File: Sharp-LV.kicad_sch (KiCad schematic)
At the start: 46 parts, among them J1 USB_C_Receptacle_USB2.0, J2 Conn_01x05_PROG, J3 5024260810, J4 FH52-10S-0.5SH_99, J5 SM04B-SRSS-TB_LF__SN_, J6 Conn_2Rows-13Pins, U1 NRF52840-QIAA-R, U2 USBLC6-2P6, U3 MCP1700-3302E_SOT23, U4 RT9080-33GJ5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

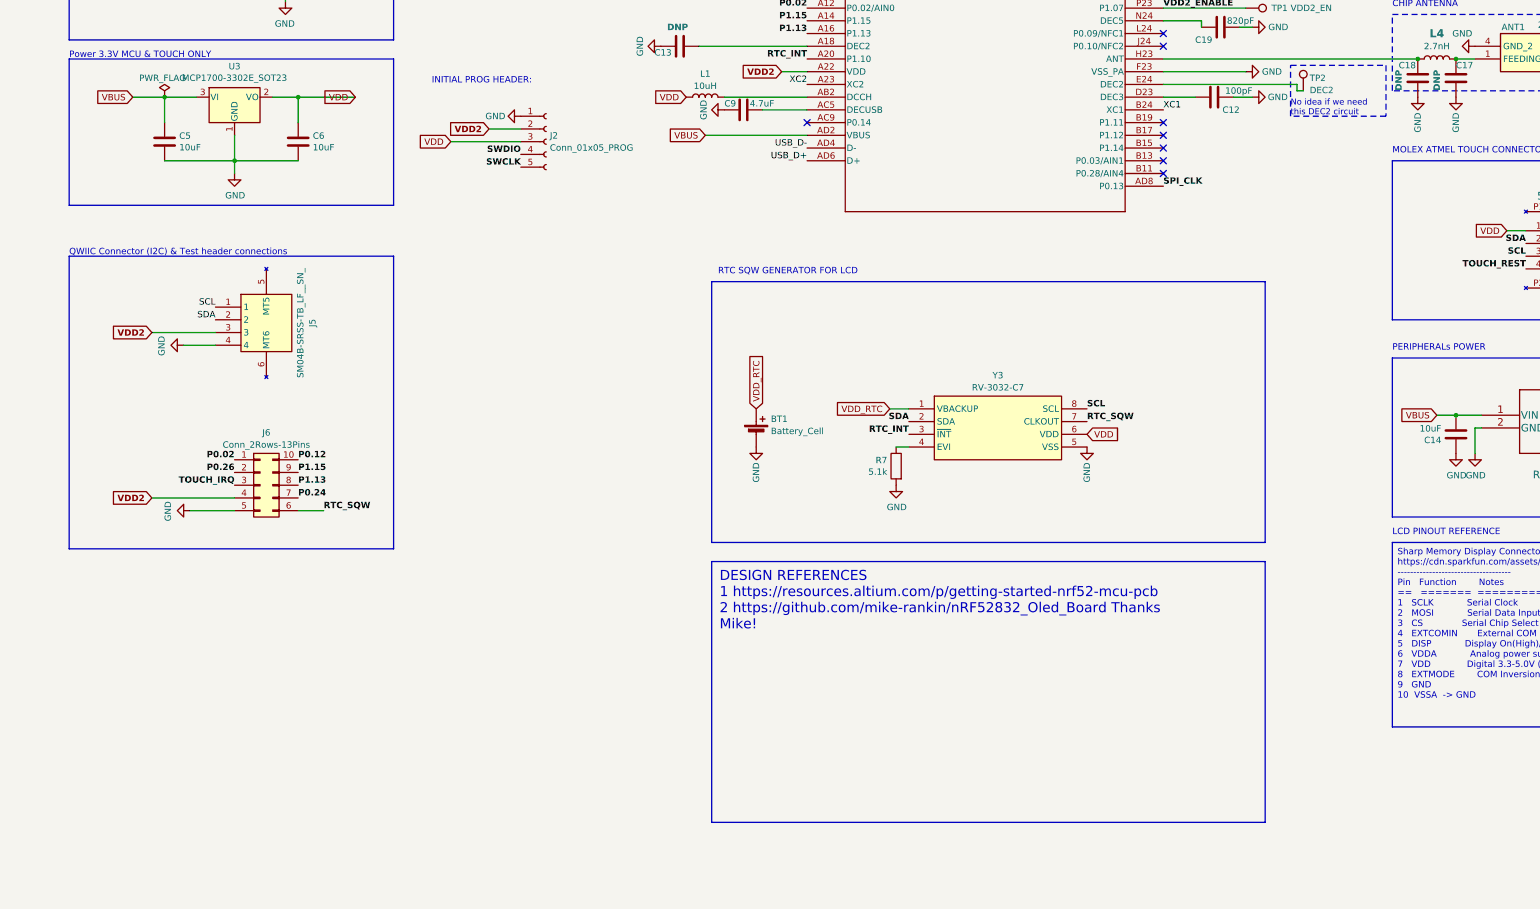
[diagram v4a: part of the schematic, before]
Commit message: Add power mux TPS2113
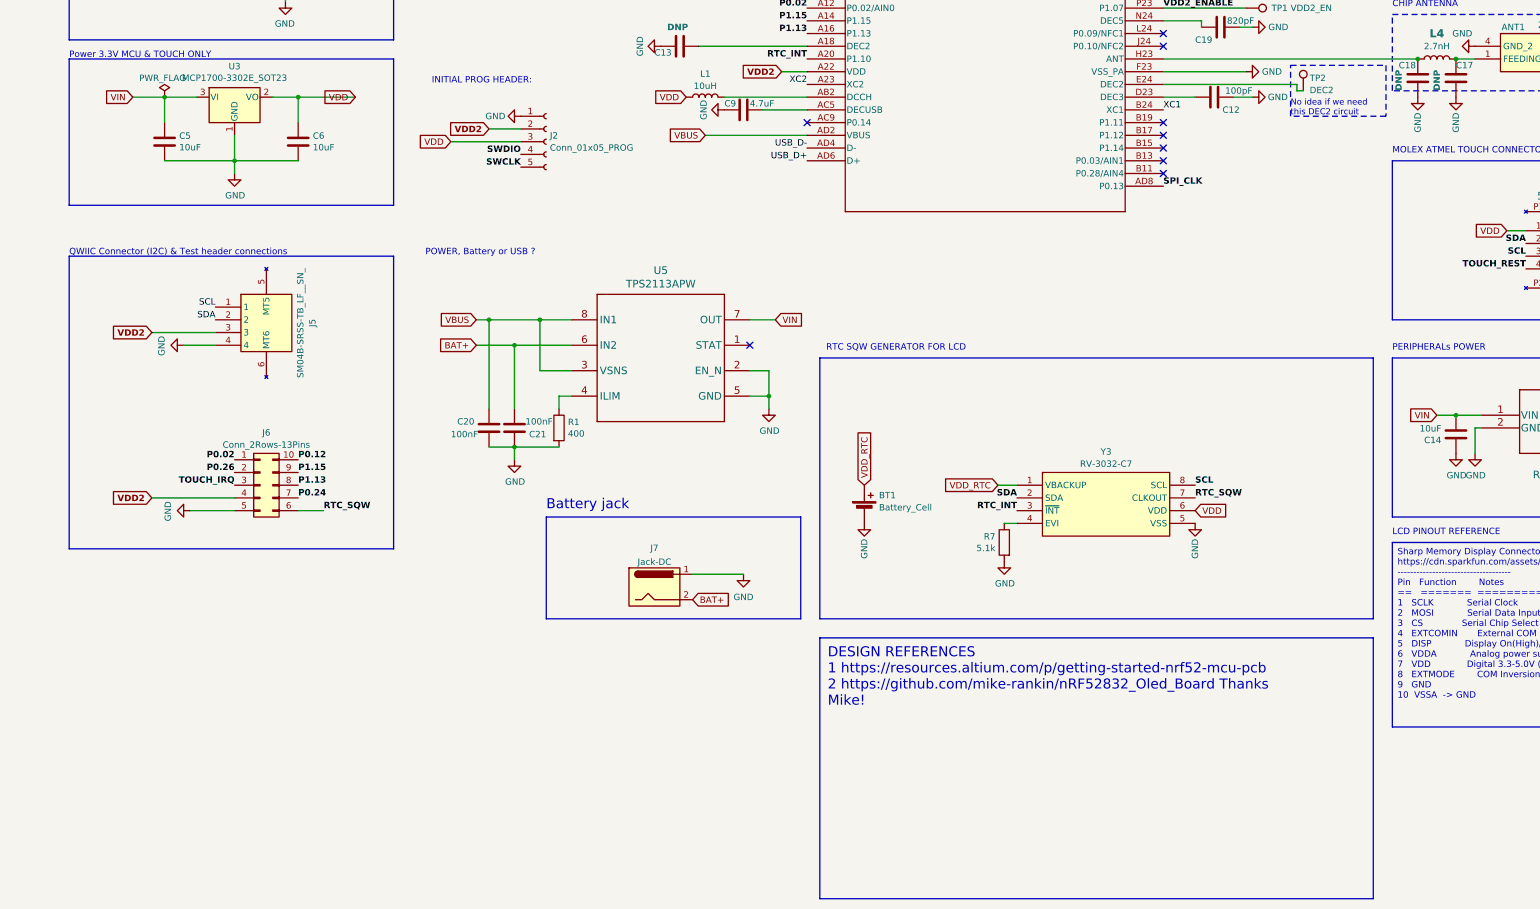
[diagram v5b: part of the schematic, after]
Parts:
- added C20, C21: 100nF, Capacitor_SMD:C_0805_2012Metric, symbol Device:C
- added J7: Jack-DC, Connector_JST:JST_LEA_SM02B-LEASS-TF_1x02-1MP_P4.20mm_Horizontal, symbol Connector:Jack-DC
- added R1: 400, Resistor_SMD:R_0603_1608Metric, symbol Device:R
- added U5: TPS2113APW, Footprints:TPS2113APWR, symbol epd_breakout:TPS2113APW
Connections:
- net GND: now also C20.2, C21.1, J7.1, R1.2, U5.2 (EN_N), U5.5 (GND)
- net VBUS: now also C20.1, U5.3 (VSNS), U5.8 (IN1); no longer C14.1, C5.2, U3.3 (VI), U4.1 (VIN)
- new net: R1.1, U5.4 (ILIM)
- new net BAT+: C21.2, J7.2, U5.6 (IN2)
- new net VIN: C14.1, C5.2, U3.3 (VI), U4.1 (VIN), U5.7 (OUT)
- no-connect marks 36 -> 37
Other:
- note added: "Battery jack"
- note added: "POWER, Battery or USB ?"
- moved on the sheet: BT1, R7, Y3

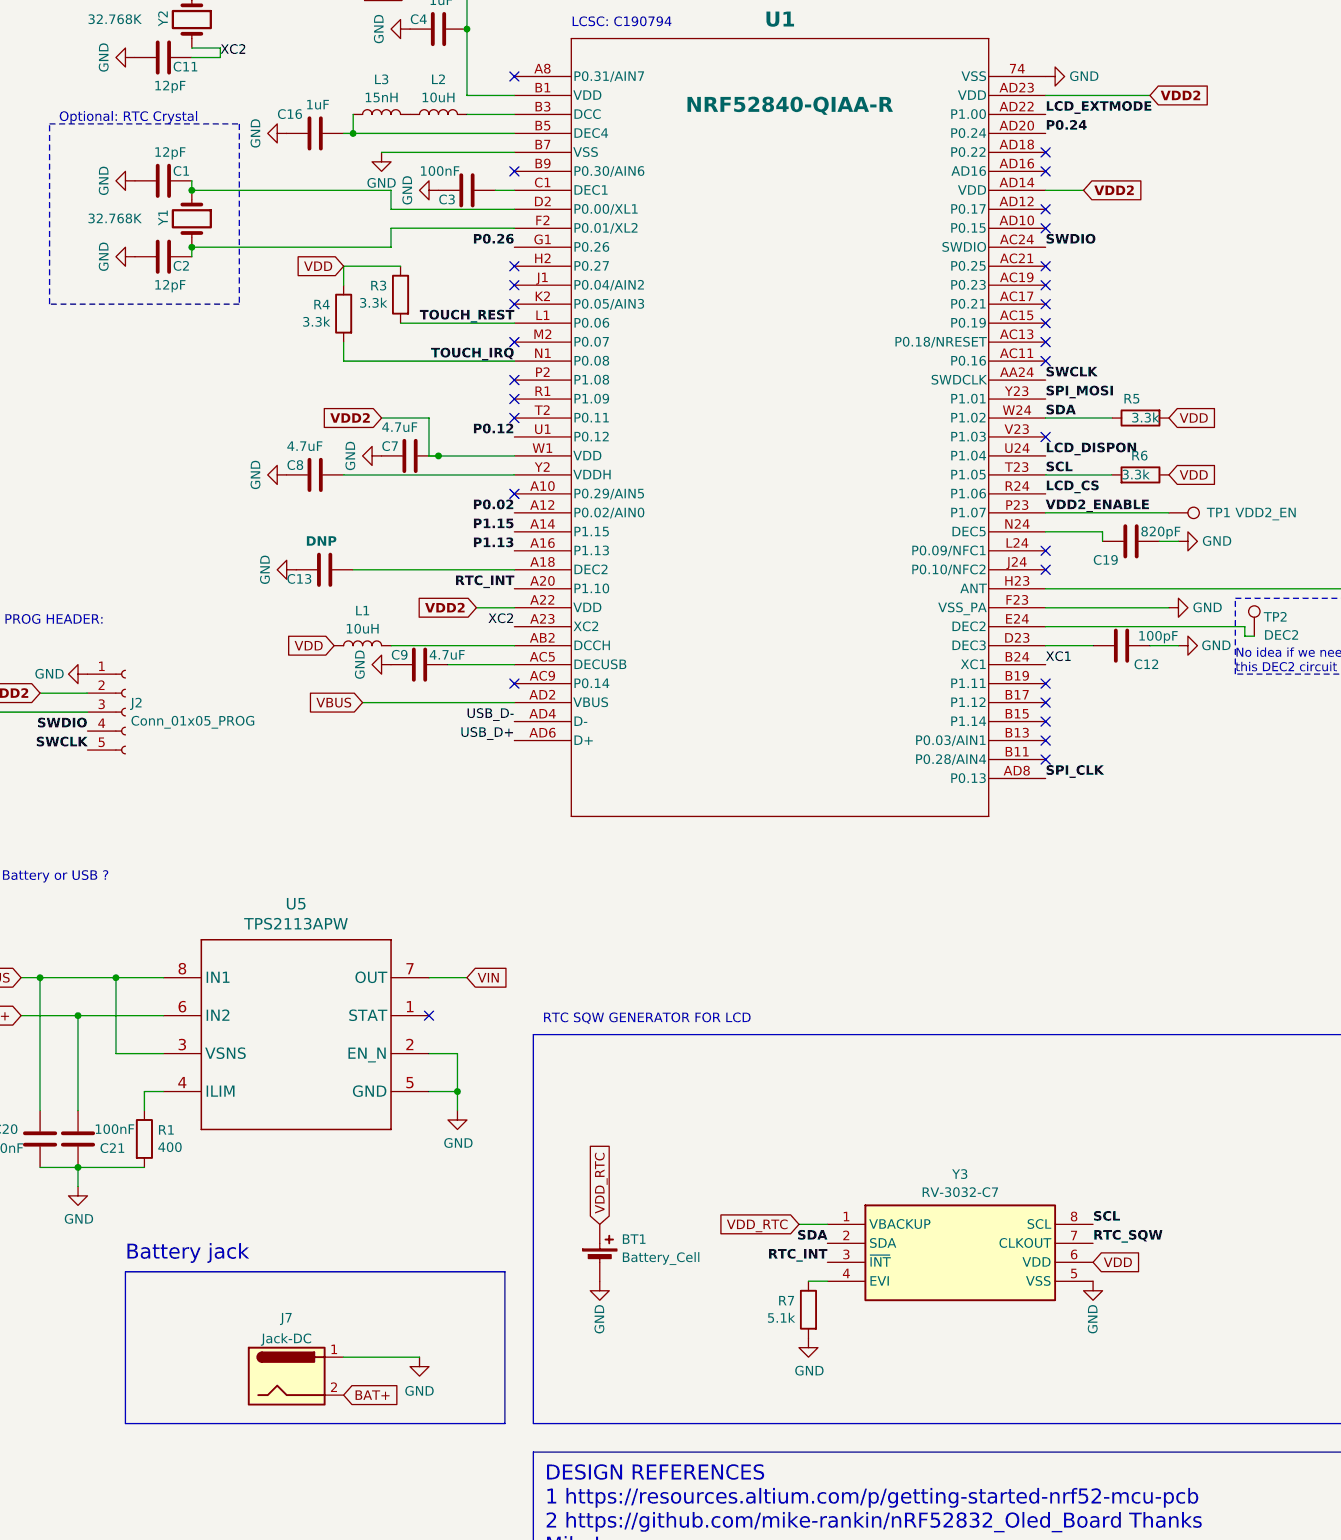
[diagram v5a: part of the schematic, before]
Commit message: Update battery connector & add SCH pdf
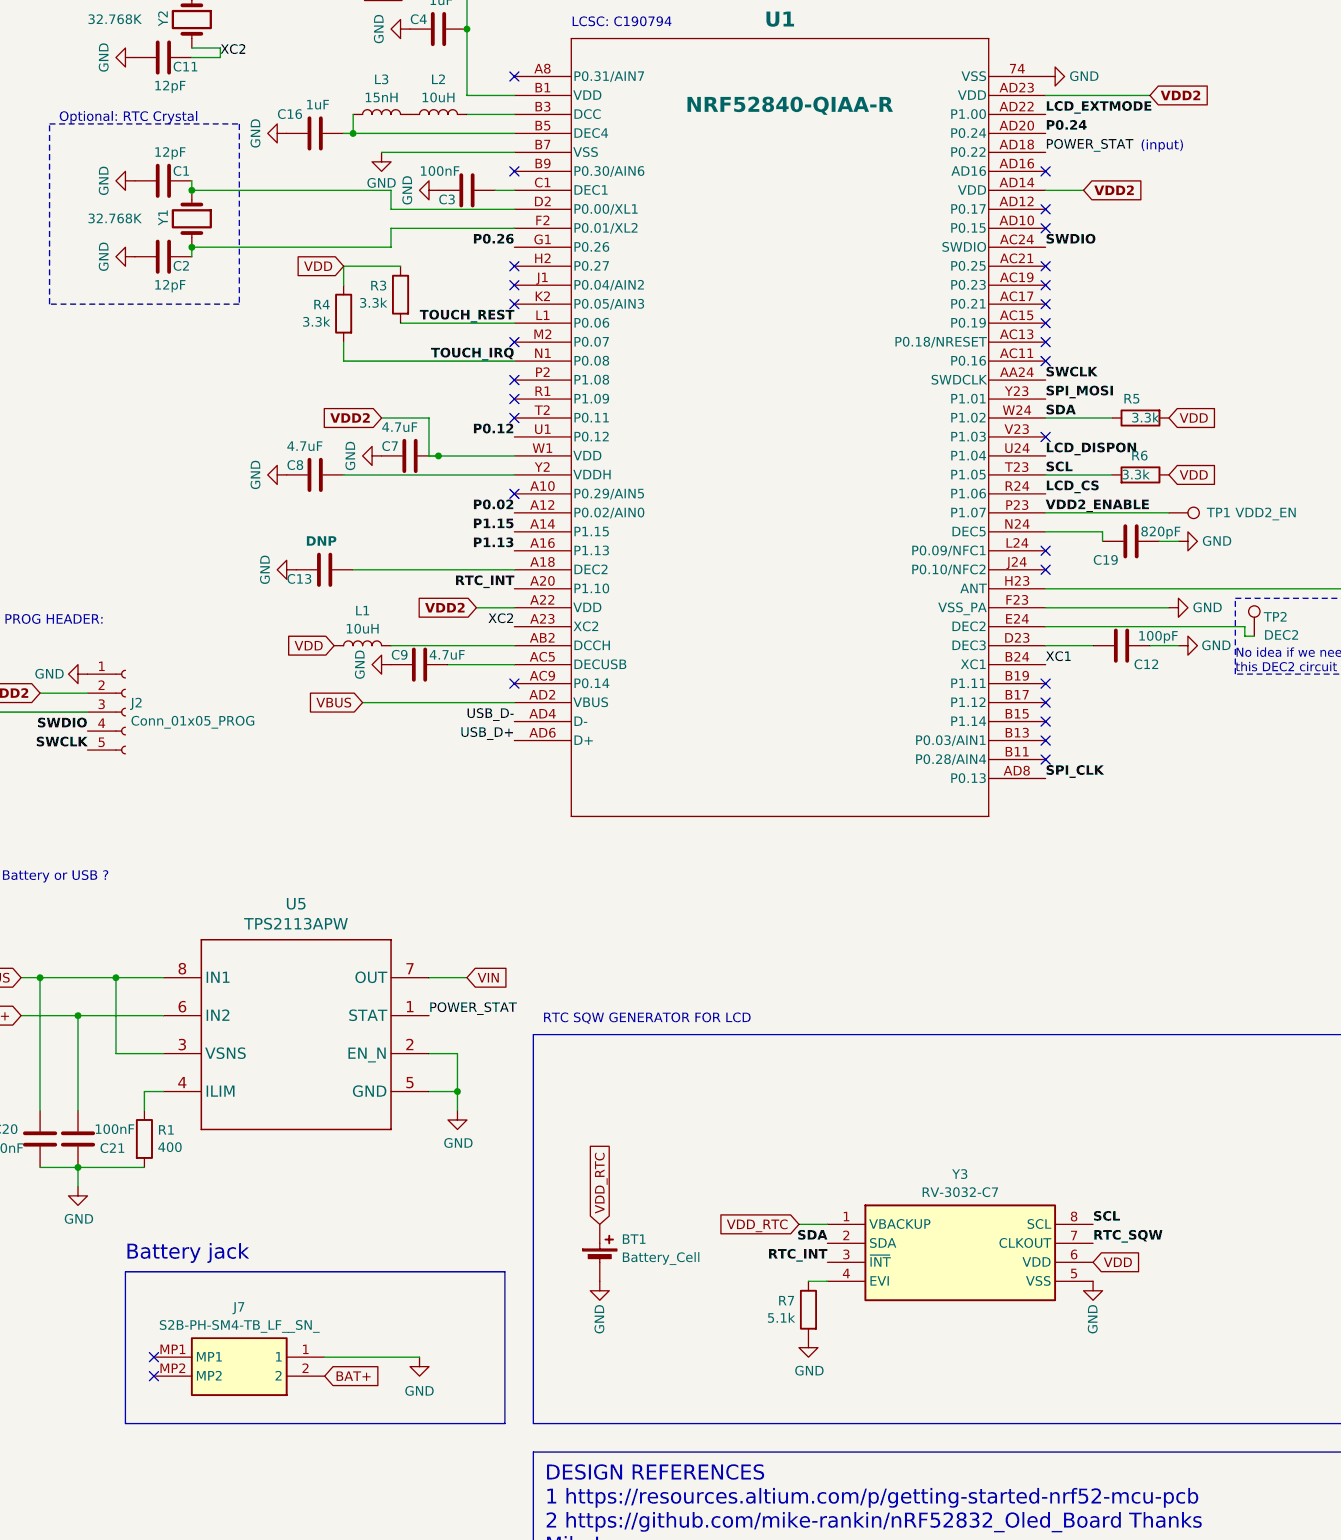
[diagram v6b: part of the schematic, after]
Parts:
- removed J7: Jack-DC, Connector_JST:JST_LEA_SM02B-LEASS-TF_1x02-1MP_P4.20mm_Horizontal, symbol Connector:Jack-DC
- added J7: S2B-PH-SM4-TB_LF__SN_, Footprints:S2BPHSM4TBLFSN, symbol Battery:S2B-PH-SM4-TB_LF__SN_
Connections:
- net BAT+: now also J7.2
- net GND: now also J7.1
- net POWER_STAT: now reaches U5.1 (STAT)
- net POWER_STAT: now also U1.AD18 (P0.22)
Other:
- note added: "(input)"
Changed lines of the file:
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@@
   (no_connect (at 251.46 80.01))
   (no_connect (at 341.63 152.4))
+  (no_connect (at 132.08 218.44))
+  (no_connect (at 132.08 215.9))
   (no_connect (at 251.46 125.73))
-  (no_connect (at 168.91 170.18))
   (no_connect (at 251.46 128.27))
   (no_connect (at 251.46 110.49))
   (no_connect (at 180.34 85.09))
-  (no_connect (at 251.46 54.61))
   (no_connect (at 180.34 80.01))
   (no_connect (at 180.34 57.15))
@@
     (stroke (width 0) (type default))
   )
-  (wire (pts (xy 157.48 215.9) (xy 167.64 215.9))
+  (wire (pts (xy 154.94 215.9) (xy 167.64 215.9))
     (stroke (width 0) (type default))
   )
@@
     (effects (font (size 1.27 1.27)) (justify left bottom))
   )
+  (text "(input)" (at 264.16 54.61 0)
+    (effects (font (size 1.27 1.27) (color 132 0 0 1)) (justify left bottom))
+  )
   (text "LCSC: C190794" (at 187.96 38.1 0)
     (effects (font (size 1.27 1.27)) (justify left bottom))
@@
     (effects (font (size 1.27 1.27) (thickness 0.254) bold (color 255 0 255 1)) (justify left bottom))
   )
+  (label "POWER_STAT" (at 168.91 170.18 0) (fields_autoplaced)
+    (effects (font (size 1.27 1.27) (color 194 0 0 1)) (justify left bottom))
+  )
   (label "SWCLK" (at 251.46 85.09 0) (fields_autoplaced)
     (effects (font (size 1.27 1.27) (thickness 0.254) bold (color 0 0 255 1)) (justify left bottom))
@@
     (effects (font (size 1.27 1.27) (thickness 0.254) bold (color 255 153 0 1)) (justify right bottom))
   )
+  (label "POWER_STAT" (at 251.46 54.61 0) (fields_autoplaced)
+    (effects (font (size 1.27 1.27) (color 194 0 0 1)) (justify left bottom))
+  )
   (label "SWDIO" (at 123.19 132.08 180) (fields_autoplaced)
     (effects (font (size 1.27 1.27) (thickness 0.254) bold (color 0 0 255 1)) (justify right bottom))
@@
     )
   )
-  (global_label "BAT+" (shape input) (at 157.48 220.98 0)
+  (global_label "BAT+" (shape input) (at 154.94 218.44 0)
     (effects (font (size 1.27 1.27)) (justify left))
-    (property "Intersheetrefs" "${INTERSHEET_REFS}" (at 157.48 220.98 0)
+    (property "Intersheetrefs" "${INTERSHEET_REFS}" (at 154.94 218.44 0)
       (effects (font (size 1.27 1.27)) hide)
     )
@@
     )
   )
-  (symbol (lib_id "Connector:Jack-DC") (at 149.86 218.44 0) (unit 1)
-    (in_bom yes) (on_board yes) (dnp no) (fields_autoplaced)
-    (property "Reference" "J7" (at 149.86 210.6635 0)
-      (effects (font (size 1.27 1.27)))
-    )
-    (property "Value" "Jack-DC" (at 149.86 213.4386 0)
-      (effects (font (size 1.27 1.27)))
-    )
-    (property "Footprint" "Connector_JST:JST_LEA_SM02B-LEASS-TF_1x02-1MP_P4.20mm_Horizontal" (at 151.13 219.456 0)
-      (effects (font (size 1.27 1.27)) hide)
-    )
-    (property "Datasheet" "~" (at 151.13 219.456 0)
-      (effects (font (size 1.27 1.27)) hide)
-    )
-    (pin "1")
-    (pin "2")
-    (instances
-      (project "Sharp-LV"
-        (path "/19808d61-e19c-42f1-b3f4-29e10270d8fb"
-          (reference "J7") (unit 1)
-        )
-      )
-    )
-  )
   (symbol (lib_id "power:GND") (at 269.24 106.68 90) (unit 1)
     (in_bom yes) (on_board yes) (dnp no) (fields_autoplaced)
@@
         )
       )
+    )
+  )
+  (symbol (lib_id "Battery:S2B-PH-SM4-TB_LF__SN_") (at 154.94 218.44 180) (unit 1)
+    (in_bom yes) (on_board yes) (dnp no) (fields_autoplaced)
+    (property "Reference" "J7" (at 143.51 209.2157 0)
+      (effects (font (size 1.27 1.27)))
+    )
+    (property "Value" "S2B-PH-SM4-TB_LF__SN_" (at 143.51 211.6399 0)
+      (effects (font (size 1.27 1.27)))
+    )
+    (property "Footprint" "Footprints:S2BPHSM4TBLFSN" (at 135.89 123.52 0)
+      (effects (font (size 1.27 1.27)) (justify left top) hide)
+    )
+    (property "Datasheet" "https://www.jst-mfg.com/product/pdf/eng/ePH.pdf" (at 135.89 23.52 0)
+      (effects (font (size 1.27 1.27)) (justify left top) hide)
+    )
+    (property "Height" "6.6" (at 135.89 -176.48 0)
+      (effects (font (size 1.27 1.27)) (justify left top) hide)
+    )
+    (property "Manufacturer_Name" "JST (JAPAN SOLDERLESS TERMINALS)" (at 135.89 -276.48 0)
+      (effects (font (size 1.27 1.27)) (justify left top) hide)
+    )
+    (property "Manufacturer_Part_Number" "S2B-PH-SM4-TB(LF)(SN)" (at 135.89 -376.48 0)
+      (effects (font (size 1.27 1.27)) (justify left top) hide)
+    )
+    (property "LCSC" "C295747" (at 135.89 -676.48 0)
+      (effects (font (size 1.27 1.27)) (justify left top) hide)
+    )
+    (pin "MP2")
+    (pin "MP1")
+    (pin "1")
+    (pin "2")
+    (instances
+      (project "Sharp-LV"
+        (path "/19808d61-e19c-42f1-b3f4-29e10270d8fb"
+          (reference "J7") (unit 1)
+        )
+      )
